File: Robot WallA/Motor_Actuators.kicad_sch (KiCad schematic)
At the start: 51 parts, among them IC9 74LVC2G241DP-Q100H, J19 22-03-5035, J20 22-03-5035, J21 22-03-5035, J22 22-03-5035, J23 Conn_01x03, J24 281695-3, J25 Conn_01x03, J26 281695-3, J27 Conn_01x03, J28 281695-3, J29 Conn_01x03, J30 39501-1002, J31 39501-1002, J32 Conn_01x03, J33 281695-3, Q4 BSS119, Q5 BSS119, U6 L298N

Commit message: Conitnue routing
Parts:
- removed C110: 100uF, SamacSys_Parts:CAPAE830X1050N, symbol SamacSys_Parts:UCH1V101MCS1GS
- added JP16, JP17: Closed, Jumper:SolderJumper-2_P1.3mm_Bridged_RoundedPad1.0x1.5mm, symbol Jumper:Jumper_2_Bridged
- Q4, Q5, R47, R49: now not fitted
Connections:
- net RX_UC: now also JP17.1 (A)
- net RX_UC_5V: now also JP17.2 (B)
- net TX_UC: now also JP16.1 (A)
- net TX_UC_5V: now also JP16.2 (B)
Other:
- moved on the sheet: C111, C112, C113, C114, R26

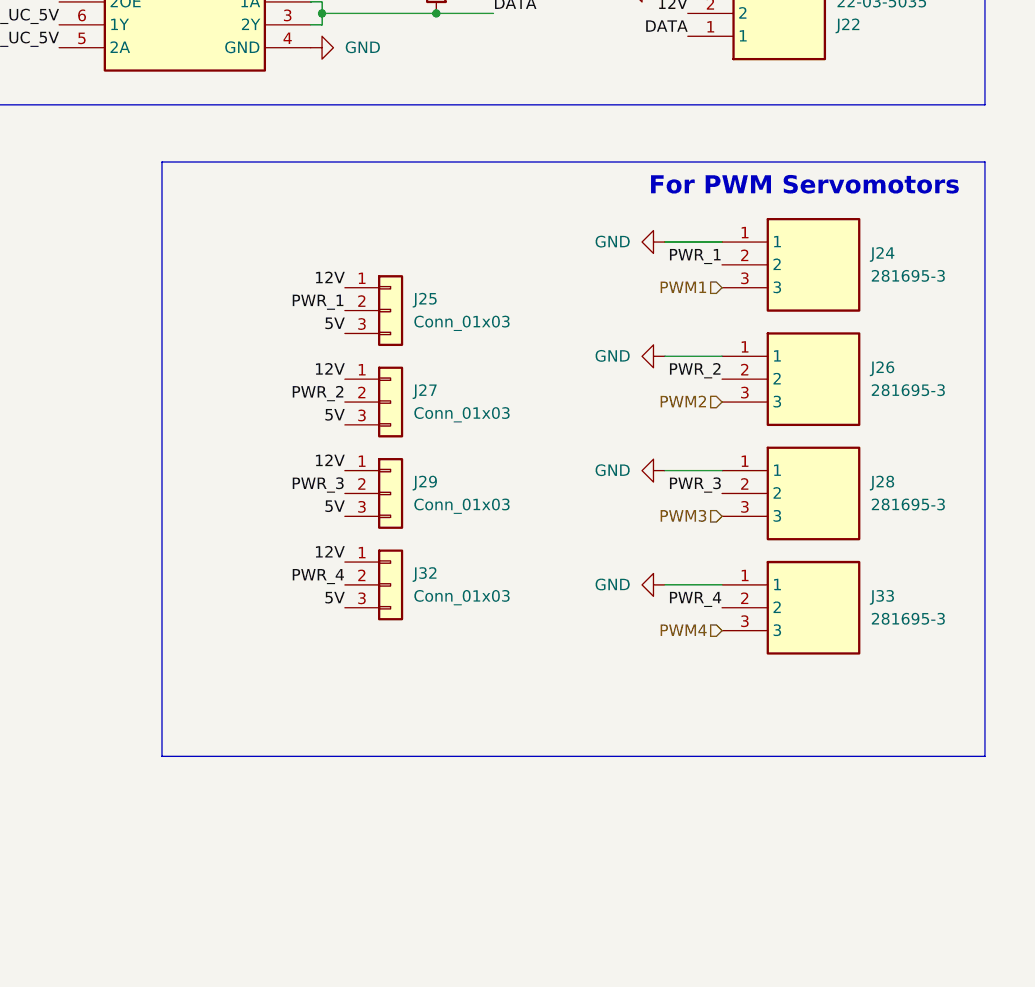
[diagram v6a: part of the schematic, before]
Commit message: Corrected all DRC erros, added info on PCB
modified distance meter connectors to be horizontal
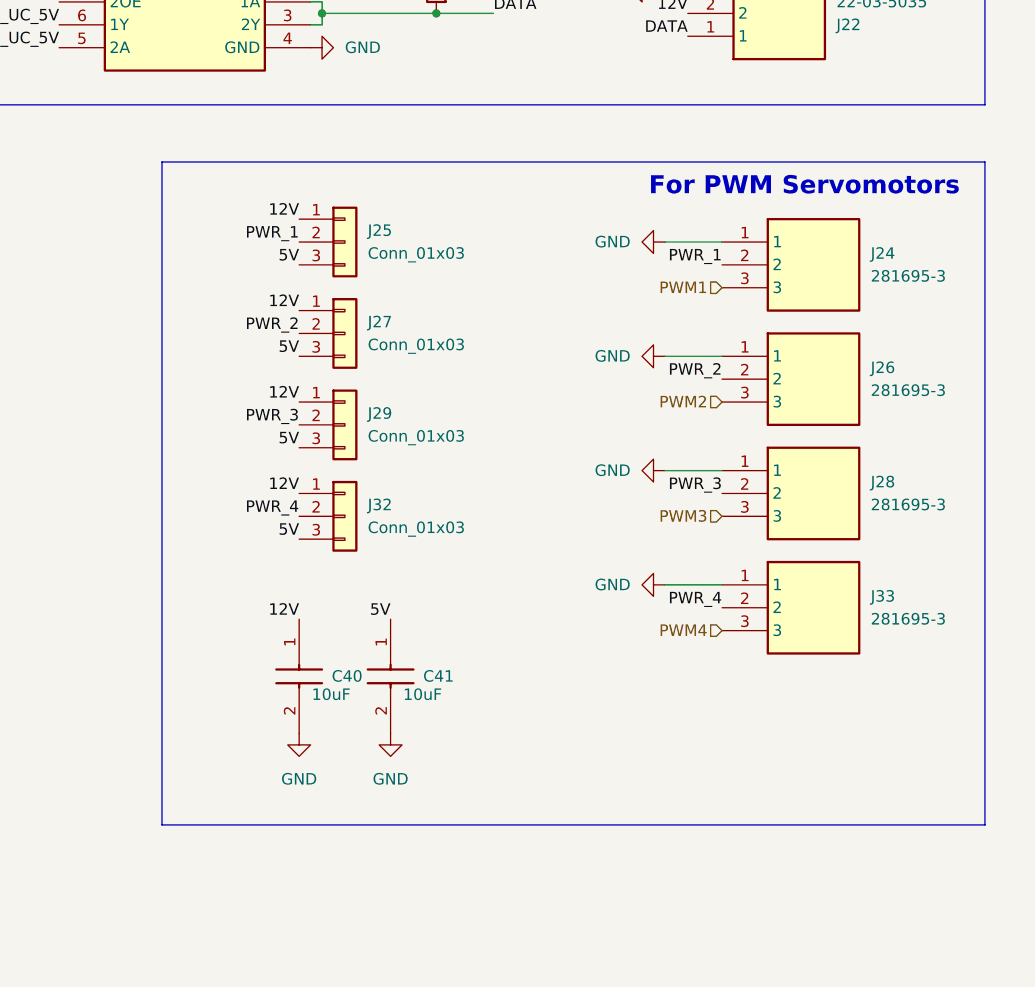
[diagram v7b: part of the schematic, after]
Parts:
- added C40, C41: 10uF, Capacitor_SMD:C_0603_1608Metric_Pad1.08x0.95mm_HandSolder, symbol SamacSys_Parts:0805DC104MAT2A
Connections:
- net 12V: now also C40.1
- net 5V: now also C41.1
- net GND: now also C40.2, C41.2
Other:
- moved on the sheet: J25, J27, J29, J32

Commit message: Updated fab files.
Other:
- company: (none) -> Socotec Monitoring
- title: (none) -> Robot Wall-A
